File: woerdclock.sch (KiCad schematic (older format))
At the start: 89 parts, among them K1 Sound, K10 WS2812B_OUT, K11 WS2812B_IN, K12 WS2812B_IN, K13 WS2812B_OUT, K14 WS2812B_OUT, K15 WS2812B_IN, K16 WS2812B_IN, K17 WS2812B_OUT, K18 WS2812B_OUT, K19 WS2812B_IN, K2 IR, K20 WS2812B_IN, K21 WS2812B_OUT, K22 WS2812B_OUT, K23 WS2812B_IN, K24 WS2812B_IN, K25 WS2812B_OUT, K26 WS2812B_OUT, K27 WS2812B_IN, K3 3V3, K4 WS2812B_OUT, K5 WS2812B_OUT, K6 WS2812B_IN, K7 WS2812B_IN, K8 WS2812B_IN, K9 WS2812B_OUT, P10 CONN_1, P11 CONN_3X2, P12 CONN_1, P13 CONN_1, P14 CONN_1, P15 CONN_1, P16 CONN_1, P17 CONN_1, P4 CONN_1, P5 CONN_1, P6 CONN_1, P7 CONN_1, P8 CONN_3X2, P9 CONN_1, SW1 up, SW2 ok, SW3 down, U1 RFM12B, U10 DCF77, U11 DHT, U14 SD-CARD, U2 RTC_MODUL, U3 ARDUINO_PRO_MICRO, U4 BH1750FVI_MODULE, U5 5V 8A -Co+, U8 ESP8266, U9 10DOF

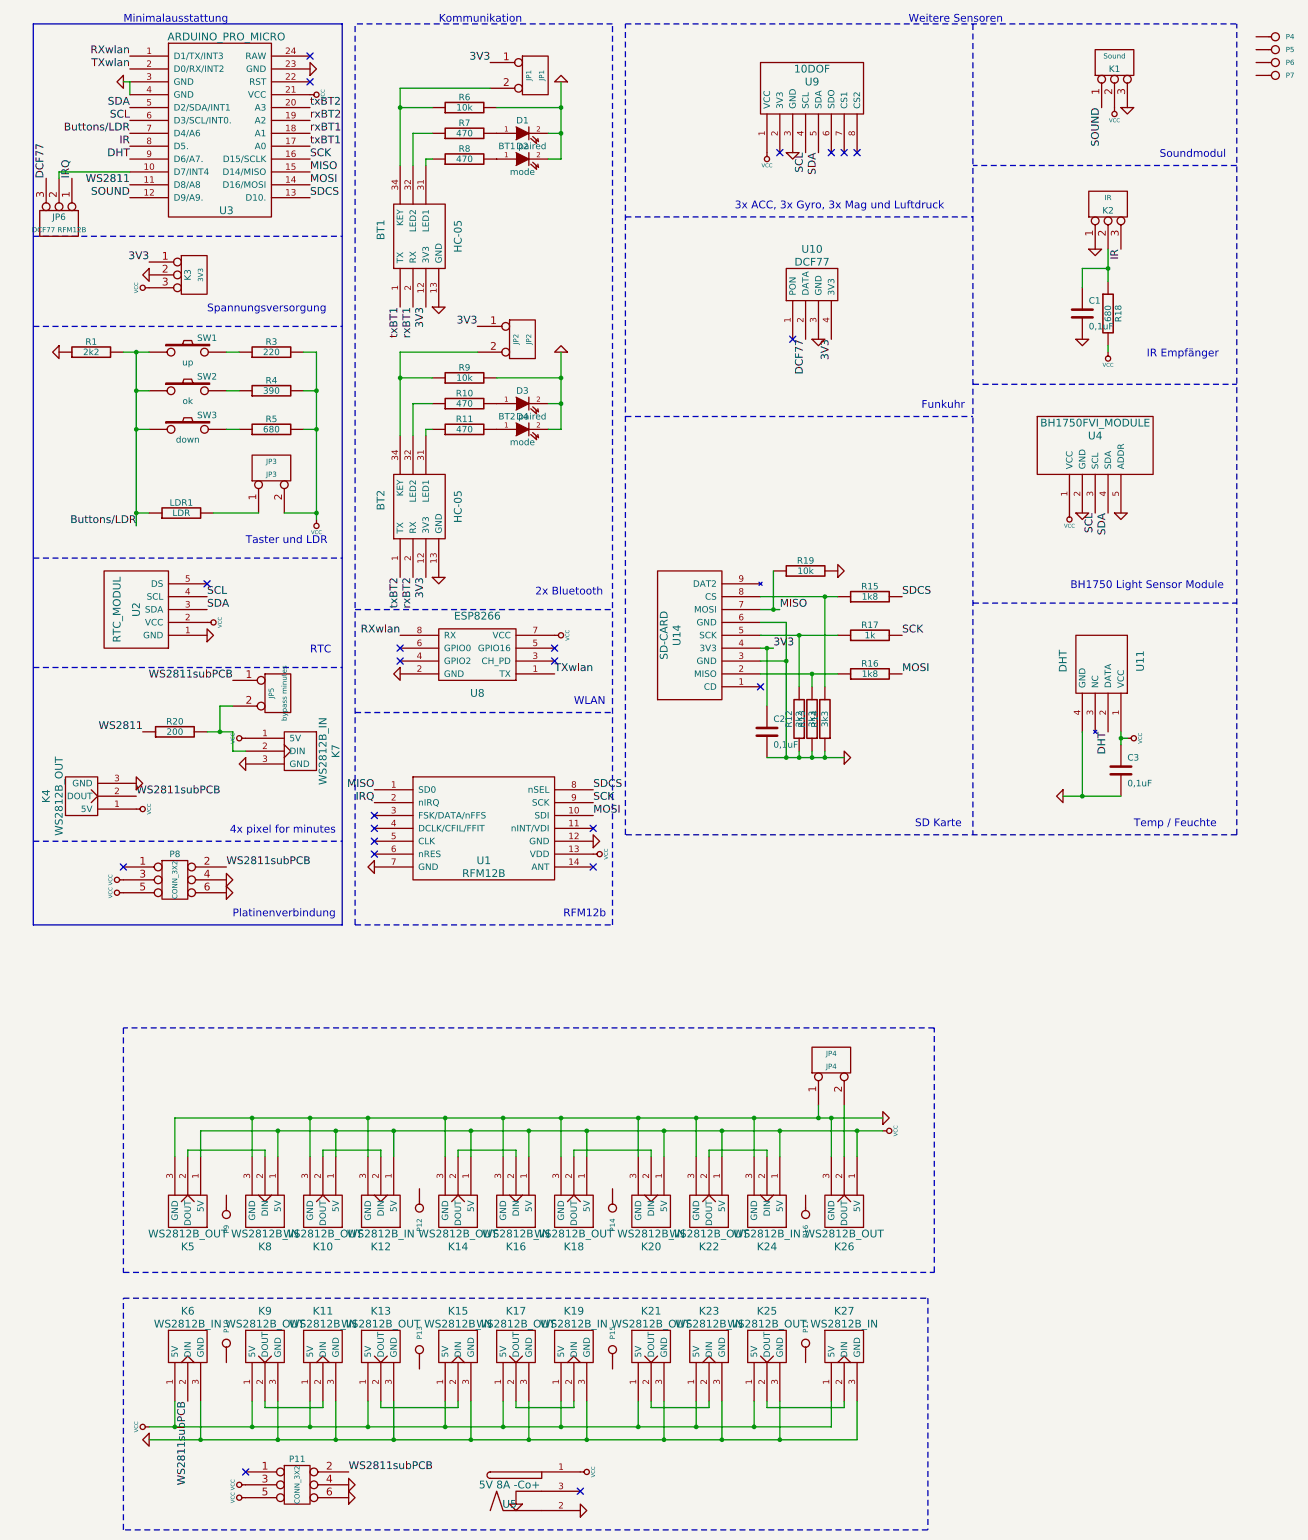
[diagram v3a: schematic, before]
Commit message: added and modified silkscreen. Footprints of BHF1750 and sound module where wrong. fixed.
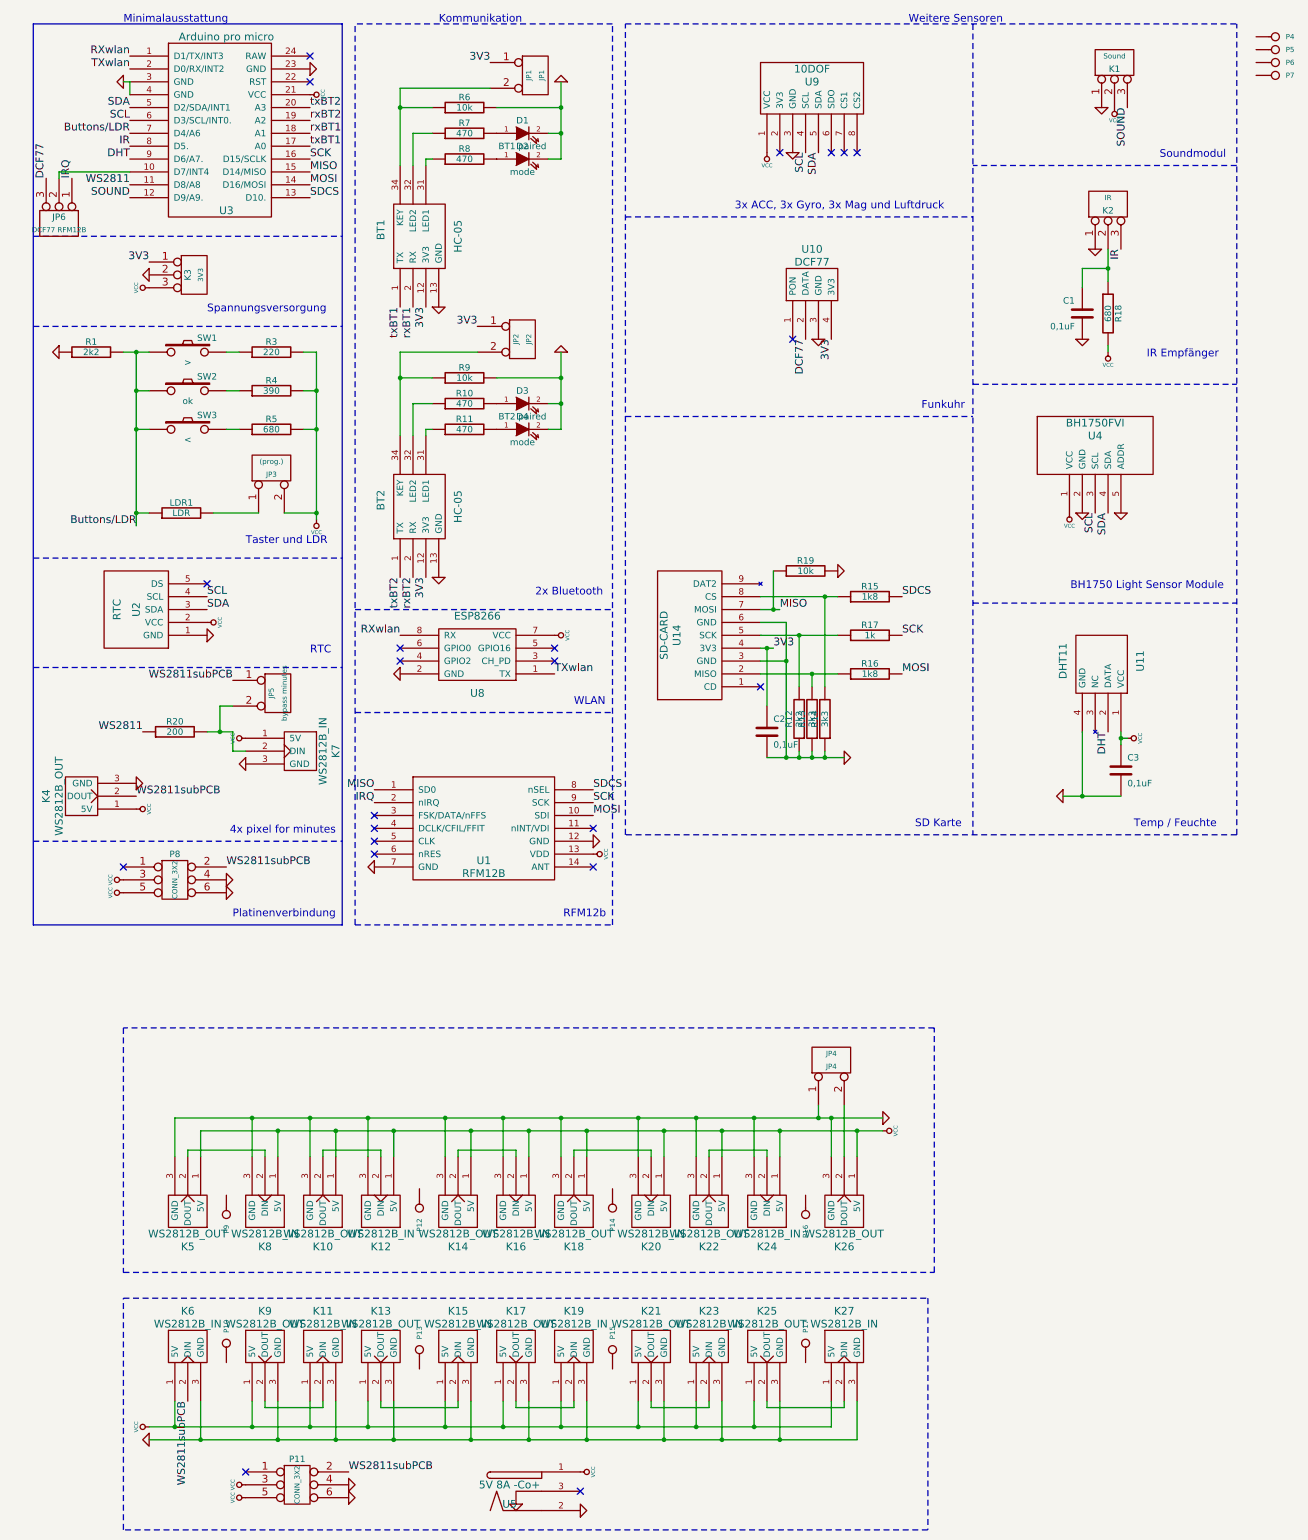
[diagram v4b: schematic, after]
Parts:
- JP3: value JP3 -> (prog.)
- SW1: value up -> >
- SW3: value down -> <
- U11: value DHT -> DHT11
- U2: value RTC_MODUL -> RTC
- U3: value ARDUINO_PRO_MICRO -> Arduino pro micro
- U4: value BH1750FVI_MODULE -> BH1750FVI
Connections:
- net GND: now also K1.1 (P1); no longer K1.3 (P3)
- net SOUND: now also K1.3 (P3); no longer K1.1 (P1)
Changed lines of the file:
@@
 Sheet 1 1
 Title "Wördclock"
-Date "22 nov 2014"
+Date "23 nov 2014"
 Rev "0.2"
 Comp "http://sebastian.setz.name"
@@
 Text Label 1350 1950 2    60   ~ 0
 SOUND
-Text Label 8900 1250 3    60   ~ 0
+Text Label 9100 1250 3    60   ~ 0
 SOUND
 $Comp
@@
 L GND #PWR06
 U 1 1 54472822
-P 9100 1250
-F 0 "#PWR06" H 9100 1250 30  0001 C CNN
-F 1 "GND" H 9100 1180 30  0001 C CNN
-F 2 "" H 9100 1250 60  0001 C CNN
-F 3 "" H 9100 1250 60  0001 C CNN
-	1    9100 1250
+P 8900 1250
+F 0 "#PWR06" H 8900 1250 30  0001 C CNN
+F 1 "GND" H 8900 1180 30  0001 C CNN
+F 2 "" H 8900 1250 60  0001 C CNN
+F 3 "" H 8900 1250 60  0001 C CNN
+	1    8900 1250
 	1    0    0    -1
 $EndComp
@@
 P 2450 4050
 F 0 "JP3" V 2400 4050 40  0000 C CNN
-F 1 "JP3" V 2500 4050 40  0000 C CNN
+F 1 "(prog.)" V 2500 4050 40  0000 C CNN
 F 2 "" H 2450 4050 60  0001 C CNN
 F 3 "" H 2450 4050 60  0001 C CNN
@@
 P 1800 3750
 F 0 "SW3" H 1950 3860 50  0000 C CNN
-F 1 "down" H 1800 3670 50  0000 C CNN
+F 1 "<" H 1800 3670 50  0000 C CNN
 F 2 "" H 1800 3750 60  0001 C CNN
 F 3 "" H 1800 3750 60  0001 C CNN
@@
 P 1800 3150
 F 0 "SW1" H 1950 3260 50  0000 C CNN
-F 1 "up" H 1800 3070 50  0000 C CNN
+F 1 ">" H 1800 3070 50  0000 C CNN
 F 2 "" H 1800 3150 60  0001 C CNN
 F 3 "" H 1800 3150 60  0001 C CNN
@@
 U 1 1 5446915B
 P 8750 2850
-F 0 "C1" H 8800 2950 50  0000 L CNN
-F 1 "0,1uF" H 8800 2750 50  0000 L CNN
+F 0 "C1" H 8600 2950 50  0000 L CNN
+F 1 "0,1uF" H 8500 2750 50  0000 L CNN
 F 2 "" H 8750 2850 60  0001 C CNN
 F 3 "" H 8750 2850 60  0001 C CNN
@@
 P 1400 5150
 F 0 "U2" H 1400 5150 60  0000 C CNN
-F 1 "RTC_MODUL" H 1400 5300 60  0000 C CNN
+F 1 "RTC" H 1400 5300 60  0000 C CNN
 F 2 "" H 1400 5150 60  0001 C CNN
 F 3 "" H 1400 5150 60  0001 C CNN
@@
 P 8900 5550
 F 0 "U11" H 8900 5850 60  0000 C CNN
-F 1 "DHT" H 8900 5250 60  0000 C CNN
+F 1 "DHT11" H 8900 5250 60  0000 C CNN
 F 2 "" H 8900 5550 60  0001 C CNN
 F 3 "" H 8900 5550 60  0001 C CNN
@@
 P 2050 1400
 F 0 "U3" H 2100 750 60  0000 C CNN
-F 1 "ARDUINO_PRO_MICRO" H 2100 2100 60  0000 C CNN
+F 1 "Arduino pro micro" H 2100 2100 60  0000 C CNN
 F 2 "" H 2050 1400 60  0000 C CNN
 F 3 "" H 2050 1400 60  0000 C CNN
@@
 P 8850 3850
 F 0 "U4" H 8850 3900 60  0000 C CNN
-F 1 "BH1750FVI_MODULE" H 8850 4000 60  0000 C CNN
+F 1 "BH1750FVI" H 8850 4000 60  0000 C CNN
 F 2 "" H 8850 3850 60  0000 C CNN
 F 3 "" H 8850 3850 60  0000 C CNN

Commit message: added capasitator on 3v3
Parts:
- added C? (x2): 0,1uF, symbol C
- added D5: ZENERSMALL, ~, symbol ZENERSMALL
- added R2: 100, symbol R
- added R21: 10k, symbol R
- R12: value 2k2 -> 3k3
- R17: value 1k -> 1k8
- R20: value 200 -> 220
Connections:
- wire segments 150 -> 165
- no-connect marks 22 -> 20
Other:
- moved on the sheet: K3, R20, U8
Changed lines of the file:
@@
 Sheet 1 1
 Title "Wördclock"
-Date "23 nov 2014"
+Date "16 dec 2014"
 Rev "0.2"
 Comp "http://sebastian.setz.name"
@@
 L CONN_3 K3
 U 1 1 5448BE8F
-P 1850 2550
-F 0 "K3" V 1800 2550 50  0000 C CNN
-F 1 "3V3" V 1900 2550 40  0000 C CNN
-F 2 "" H 1850 2550 60  0001 C CNN
-F 3 "" H 1850 2550 60  0001 C CNN
-	1    1850 2550
+P 1850 2600
+F 0 "K3" V 1800 2600 50  0000 C CNN
+F 1 "3V3" V 1900 2600 40  0000 C CNN
+F 2 "" H 1850 2600 60  0001 C CNN
+F 3 "" H 1850 2600 60  0001 C CNN
+	1    1850 2600
 	1    0    0    -1
 $EndComp
@@
 L VCC #PWR03
 U 1 1 5448AD7C
-P 1500 2650
-F 0 "#PWR03" H 1500 2750 30  0001 C CNN
-F 1 "VCC" H 1500 2750 30  0000 C CNN
-F 2 "" H 1500 2650 60  0001 C CNN
-F 3 "" H 1500 2650 60  0001 C CNN
-	1    1500 2650
+P 950 2600
+F 0 "#PWR03" H 950 2700 30  0001 C CNN
+F 1 "VCC" H 950 2700 30  0000 C CNN
+F 2 "" H 950 2600 60  0001 C CNN
+F 3 "" H 950 2600 60  0001 C CNN
+	1    950  2600
 	0    -1   -1   0
 $EndComp
@@
 Text Label 1350 1850 2    60   ~ 0
 WS2811
-Text Label 1450 6100 2    60   ~ 0
+Text Label 1400 6250 2    60   ~ 0
 WS2811
 Text Label 1350 1450 2    60   ~ 0
@@
 P 6550 6000
 F 0 "R12" V 6630 6000 50  0000 C CNN
-F 1 "2k2" V 6550 6000 50  0000 C CNN
+F 1 "3k3" V 6550 6000 50  0000 C CNN
 F 2 "" H 6550 6000 60  0001 C CNN
 F 3 "" H 6550 6000 60  0001 C CNN
@@
 P 7100 5350
 F 0 "R17" V 7180 5350 50  0000 C CNN
-F 1 "1k" V 7100 5350 50  0000 C CNN
+F 1 "1k8" V 7100 5350 50  0000 C CNN
 F 2 "" H 7100 5350 60  0001 C CNN
 F 3 "" H 7100 5350 60  0001 C CNN
@@
 L GND #PWR012
 U 1 1 5446A833
-P 1500 2550
-F 0 "#PWR012" H 1500 2550 30  0001 C CNN
-F 1 "GND" H 1500 2480 30  0001 C CNN
-F 2 "" H 1500 2550 60  0001 C CNN
-F 3 "" H 1500 2550 60  0001 C CNN
-	1    1500 2550
-	0    1    1    0
+P 1550 2400
+F 0 "#PWR012" H 1550 2400 30  0001 C CNN
+F 1 "GND" H 1550 2330 30  0001 C CNN
+F 2 "" H 1550 2400 60  0001 C CNN
+F 3 "" H 1550 2400 60  0001 C CNN
+	1    1550 2400
+	0    -1   -1   0
 $EndComp
 $Comp
@@
 	0    1    1    0
 $EndComp
-Text Label 1500 2450 2    60   ~ 0
+Text Label 950  2700 2    60   ~ 0
 3V3
 Text Label 6800 3050 3    60   ~ 0
@@
 Text Label 9050 2350 3    60   ~ 0
 IR
-Text Label 8950 6100 3    60   ~ 0
+Text Label 8650 6350 3    60   ~ 0
 DHT
 $Comp
@@
 L VCC #PWR018
 U 1 1 54469F3B
-P 4650 5350
-F 0 "#PWR018" H 4650 5450 30  0001 C CNN
-F 1 "VCC" H 4650 5450 30  0000 C CNN
-F 2 "" H 4650 5350 60  0001 C CNN
-F 3 "" H 4650 5350 60  0001 C CNN
-	1    4650 5350
+P 4950 5350
+F 0 "#PWR018" H 4950 5450 30  0001 C CNN
+F 1 "VCC" H 4950 5450 30  0000 C CNN
+F 2 "" H 4950 5350 60  0001 C CNN
+F 3 "" H 4950 5350 60  0001 C CNN
+	1    4950 5350
 	0    1    1    0
 $EndComp
@@
 L GND #PWR019
 U 1 1 54469F29
-P 3450 5650
-F 0 "#PWR019" H 3450 5650 30  0001 C CNN
-F 1 "GND" H 3450 5580 30  0001 C CNN
-F 2 "" H 3450 5650 60  0001 C CNN
-F 3 "" H 3450 5650 60  0001 C CNN
-	1    3450 5650
+P 3350 5650
+F 0 "#PWR019" H 3350 5650 30  0001 C CNN
+F 1 "GND" H 3350 5580 30  0001 C CNN
+F 2 "" H 3350 5650 60  0001 C CNN
+F 3 "" H 3350 5650 60  0001 C CNN
+	1    3350 5650
 	0    1    1    0
 $EndComp
@@
 	1    0    0    -1
 $EndComp
-Text Label 4650 5650 0    60   ~ 0
+Text Label 4800 5650 0    60   ~ 0
 TXwlan
-Text Label 3450 5350 2    60   ~ 0
+Text Label 3300 5850 0    60   ~ 0
 RXwlan
 Text Label 3450 2800 3    60   ~ 0
@@
 Text Label 2750 1250 0    60   ~ 0
 txBT2
-NoConn ~ 3450 5450
-NoConn ~ 3450 5550
-NoConn ~ 4650 5450
-NoConn ~ 4650 5550
+NoConn ~ 3600 5450
+NoConn ~ 3600 5550
 $Comp
 L GND #PWR027
@@
 L ESP8266 U8
 U 1 1 5446588F
-P 4050 5500
-F 0 "U8" H 4050 5800 60  0000 C CNN
-F 1 "ESP8266" H 4050 5200 60  0000 C CNN
-F 2 "" H 4050 5500 60  0001 C CNN
-F 3 "" H 4050 5500 60  0001 C CNN
-	1    4050 5500
+P 4200 5500
+F 0 "U8" H 4200 5800 60  0000 C CNN
+F 1 "ESP8266" H 4200 5200 60  0000 C CNN
+F 2 "" H 4200 5500 60  0001 C CNN
+F 3 "" H 4200 5500 60  0001 C CNN
+	1    4200 5500
 	-1   0    0    1
 $EndComp
@@
 L R R20
 U 1 1 546B02B7
-P 1700 6100
-F 0 "R20" V 1780 6100 50  0000 C CNN
-F 1 "200" V 1700 6100 50  0000 C CNN
-F 2 "" H 1700 6100 60  0001 C CNN
-F 3 "" H 1700 6100 60  0001 C CNN
-	1    1700 6100
+P 1650 6250
+F 0 "R20" V 1730 6250 50  0000 C CNN
+F 1 "220" V 1650 6250 50  0000 C CNN
+F 2 "" H 1650 6250 60  0001 C CNN
+F 3 "" H 1650 6250 60  0001 C CNN
+	1    1650 6250
 	0    -1   -1   0
 $EndComp
@@
 	2150 5900 2050 5900
 Wire Wire Line
-	2050 5900 2050 6100
+	2050 5900 2050 6250
 $Comp
 L CONN_3 JP6
@@
 NoConn ~ 4850 12000
 Wire Wire Line
-	1950 6100 2150 6100
-Wire Wire Line
-	2150 6100 2150 6250
-Wire Wire Line
-	2150 6250 2250 6250
-Connection ~ 2050 6100
+	1900 6250 2250 6250
+Connection ~ 2050 6250
+Wire Wire Line
+	4900 5550 4800 5550
+Wire Wire Line
+	4900 5350 4900 5550
+Wire Wire Line
+	4800 5350 4950 5350
+Connection ~ 4900 5350
+Wire Wire Line
+	4800 5450 4900 5450
+Connection ~ 4900 5450
+$Comp
+L ZENERSMALL D5
+U 1 1 547736CF
+P 3450 5450
+F 0 "D5" H 3450 5550 40  0000 C CNN
+F 1 "ZENERSMALL" H 3450 5350 30  0000 C CNN
+F 2 "~" H 3450 5450 60  0000 C CNN
+F 3 "~" H 3450 5450 60  0000 C CNN
+	1    3450 5450
+	0    -1   -1   0
+$EndComp
+Wire Wire Line
+	3200 5350 3600 5350
+Connection ~ 3450 5350
+Wire Wire Line
+	3350 5650 3600 5650
+Wire Wire Line
+	3450 5550 3450 5650
+Connection ~ 3450 5650
+Wire Wire Line
+	3200 5850 3300 5850
+$Comp
+L R R2
+U 1 1 54773EC9
+P 3200 5600
+F 0 "R2" V 3280 5600 50  0000 C CNN
+F 1 "100" V 3200 5600 50  0000 C CNN
+F 2 "" H 3200 5600 60  0001 C CNN
+F 3 "" H 3200 5600 60  0001 C CNN
+	1    3200 5600
+	-1   0    0    1
+$EndComp
+$Comp
+L R R21
+U 1 1 54860AC0
+P 8400 6200
+F 0 "R21" V 8480 6200 50  0000 C CNN
+F 1 "10k" V 8400 6200 50  0000 C CNN
+F 2 "" H 8400 6200 60  0001 C CNN
+F 3 "" H 8400 6200 60  0001 C CNN
+	1    8400 6200
+	0    -1   -1   0
+$EndComp
+Wire Wire Line
+	8950 6100 8950 6200
+Wire Wire Line
+	8950 6200 8650 6200
+Wire Wire Line
+	8650 6200 8650 6350
+$Comp
+L VCC #PWR052
+U 1 1 54860CD8
+P 8150 6200
+F 0 "#PWR052" H 8150 6300 30  0001 C CNN
+F 1 "VCC" H 8150 6300 30  0000 C CNN
+F 2 "" H 8150 6200 60  0001 C CNN
+F 3 "" H 8150 6200 60  0001 C CNN
+	1    8150 6200
+	0    -1   -1   0
+$EndComp
+$Comp
+L C C?
+U 1 1 549009D8
+P 1300 2850
+F 0 "C?" H 1350 2950 50  0000 L CNN
+F 1 "0,1uF" H 1350 2750 50  0000 L CNN
+F 2 "" H 1300 2850 60  0001 C CNN
+F 3 "" H 1300 2850 60  0001 C CNN
+	1    1300 2850
+	0    -1   -1   0
+$EndComp
+$Comp
+L C C?
+U 1 1 549009DE
+P 1200 2400
+F 0 "C?" H 1250 2500 50  0000 L CNN
+F 1 "0,1uF" H 1250 2300 50  0000 L CNN
+F 2 "" H 1200 2400 60  0001 C CNN
+F 3 "" H 1200 2400 60  0001 C CNN
+	1    1200 2400
+	0    -1   -1   0
+$EndComp
+Wire Wire Line
+	1500 2850 1500 2700
+Wire Wire Line
+	1500 2700 950  2700
+$Comp
+L GND #PWR?
+U 1 1 54900C53
+P 1100 2850
+F 0 "#PWR?" H 1100 2850 30  0001 C CNN
+F 1 "GND" H 1100 2780 30  0001 C CNN
+F 2 "" H 1100 2850 60  0001 C CNN
+F 3 "" H 1100 2850 60  0001 C CNN
+	1    1100 2850
+	0    1    1    0
+$EndComp
+Wire Wire Line
+	1500 2600 950  2600
+Wire Wire Line
+	1000 2400 1000 2600
+Connection ~ 1000 2600
+Wire Wire Line
+	1400 2400 1550 2400
+Wire Wire Line
+	1500 2400 1500 2500
+Connection ~ 1500 2400
 $EndSCHEMATC

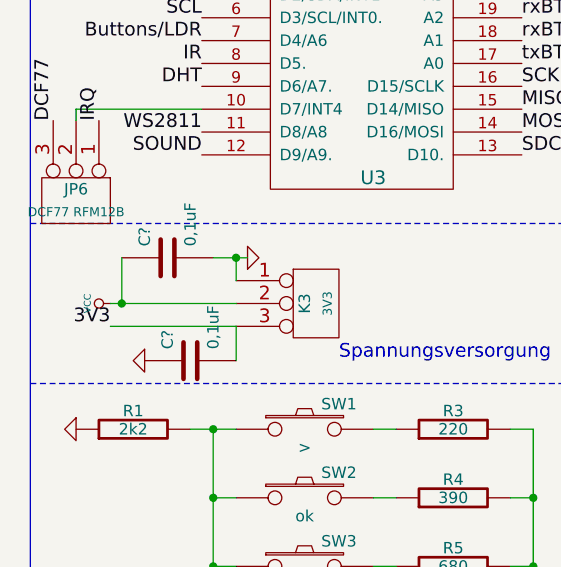
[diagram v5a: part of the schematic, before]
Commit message: added capasitator on 3v3
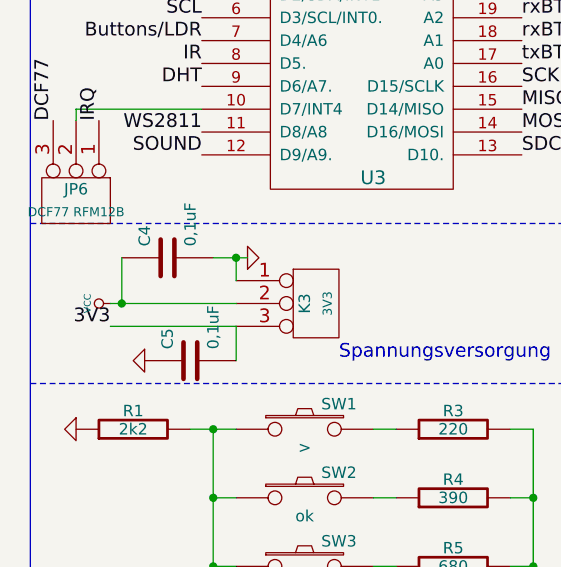
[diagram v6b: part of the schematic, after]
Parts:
- gave numbers to parts that had none: 2
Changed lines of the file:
@@
 $EndComp
 $Comp
-L C C?
+L C C5
 U 1 1 549009D8
 P 1300 2850
-F 0 "C?" H 1350 2950 50  0000 L CNN
+F 0 "C5" H 1350 2950 50  0000 L CNN
 F 1 "0,1uF" H 1350 2750 50  0000 L CNN
 F 2 "" H 1300 2850 60  0001 C CNN
@@
 $EndComp
 $Comp
-L C C?
+L C C4
 U 1 1 549009DE
 P 1200 2400
-F 0 "C?" H 1250 2500 50  0000 L CNN
+F 0 "C4" H 1250 2500 50  0000 L CNN
 F 1 "0,1uF" H 1250 2300 50  0000 L CNN
 F 2 "" H 1200 2400 60  0001 C CNN
@@
 	1500 2700 950  2700
 $Comp
-L GND #PWR?
+L GND #PWR053
 U 1 1 54900C53
 P 1100 2850
-F 0 "#PWR?" H 1100 2850 30  0001 C CNN
+F 0 "#PWR053" H 1100 2850 30  0001 C CNN
 F 1 "GND" H 1100 2780 30  0001 C CNN
 F 2 "" H 1100 2850 60  0001 C CNN
